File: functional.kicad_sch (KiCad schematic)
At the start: 12 parts, among them SW1 PCM12SMTR, U2 APX803L20-29SA-7, U3 PL500-37TC, Y1 XRCGB32M000F2P01R0

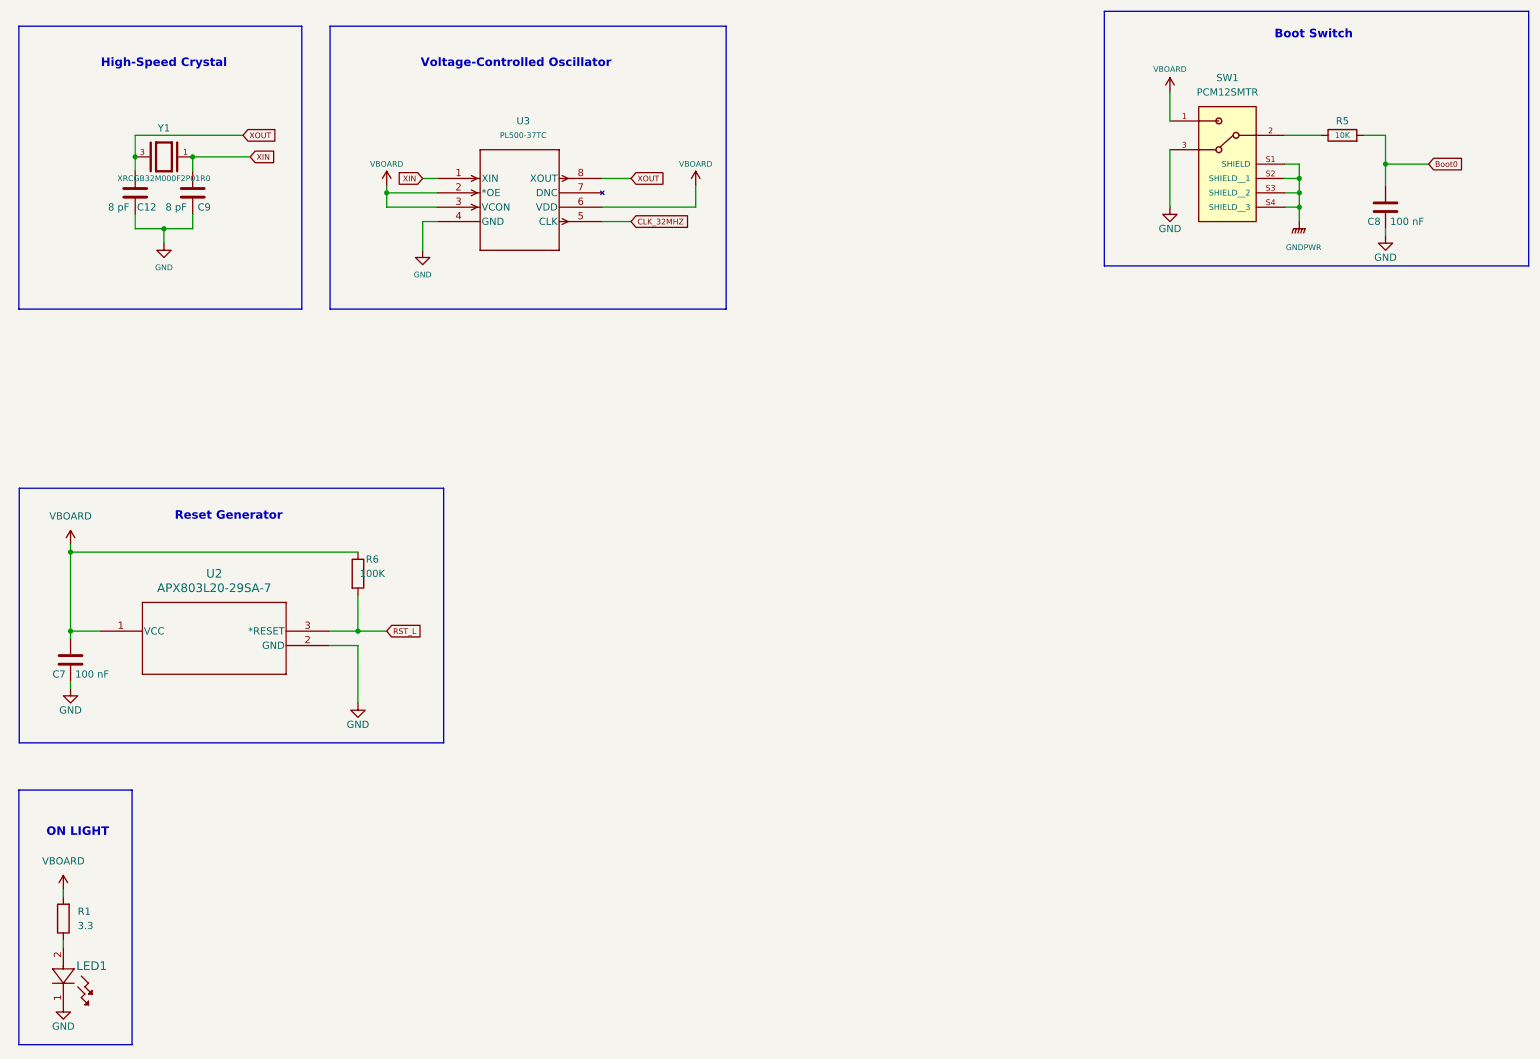
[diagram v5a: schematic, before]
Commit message: separated voltage source labels
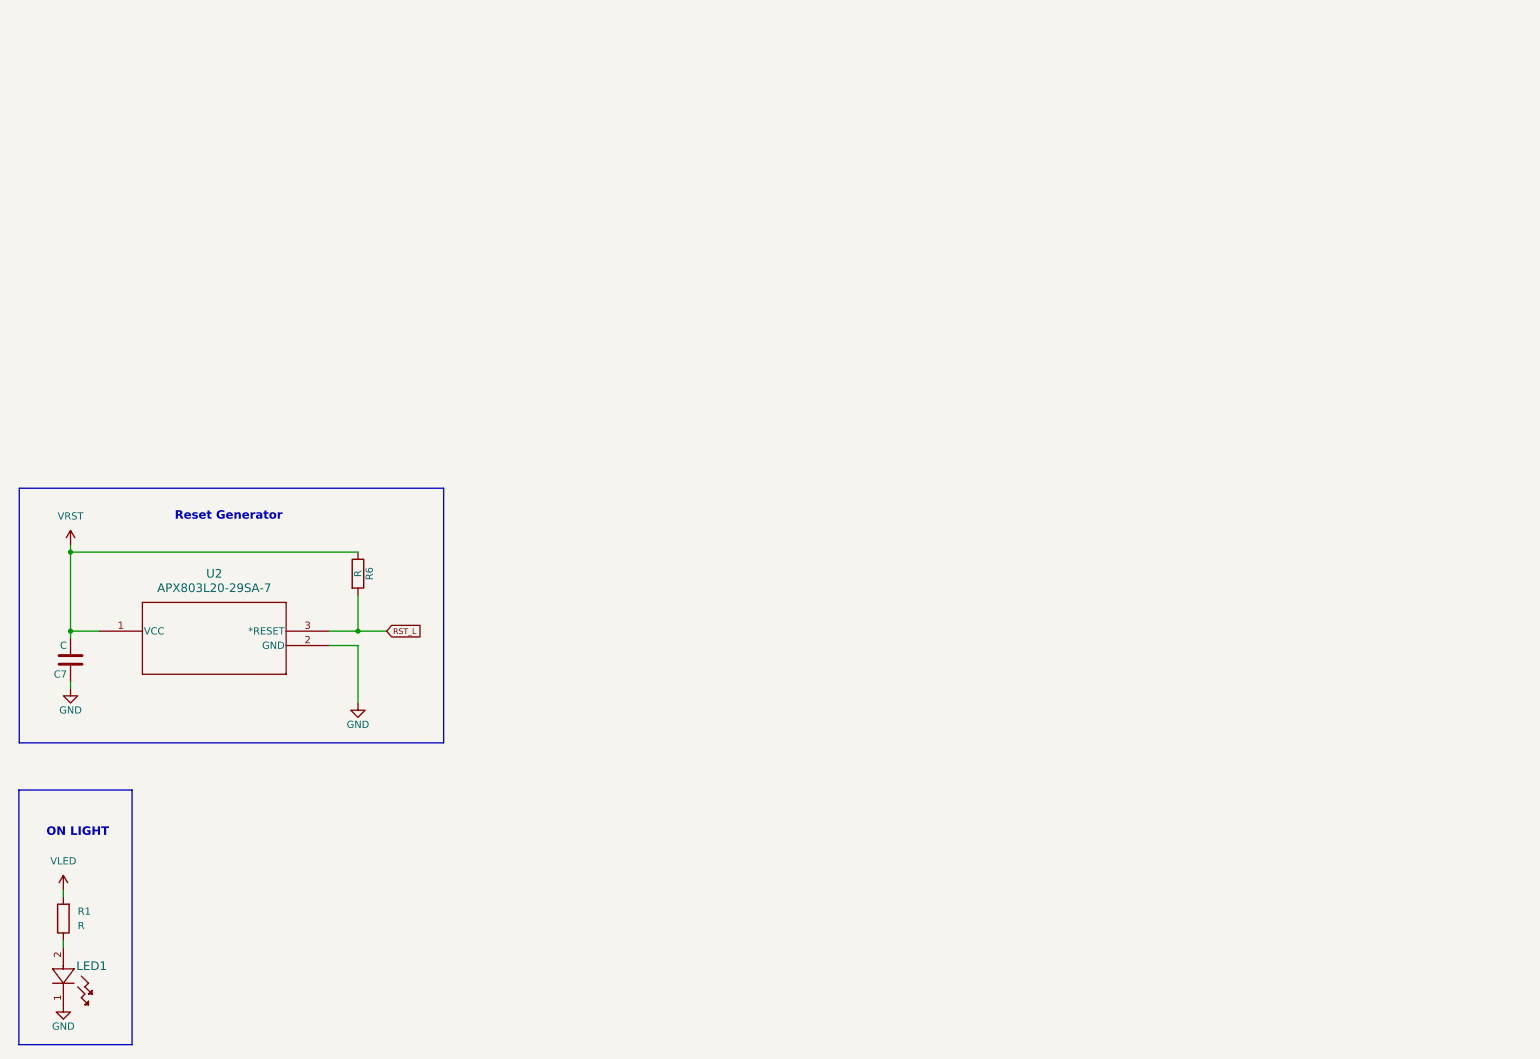
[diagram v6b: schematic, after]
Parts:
- removed C12, C9: 8 pF, Capacitor_SMD:C_0805_2012Metric, symbol Device:C
- removed C8: 100 nF, Capacitor_SMD:C_0805_2012Metric, symbol Device:C
- removed R5: 10K, Resistor_SMD:R_0805_2012Metric, symbol Device:R
- removed SW1: PCM12SMTR, PCM12SMTR:PCM12SMTR_CNK, symbol PCM12SMTR:PCM12SMTR
- removed U3: PL500-37TC, SOP-8_MCH, symbol VCO_36MHZ:PL500-37TC
- removed Y1: XRCGB32M000F2P01R0, XRCGB32M000F2P01R0:OSC_XRCGB32M000F2P01R0, symbol XRCGB32M000F2P01R0:XRCGB32M000F2P01R0
- C7: value 100 nF -> C
- R1: value 3.3 -> R
- R6: value 100K -> R
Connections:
- net VBOARD renamed VRST
- net VRST: no longer R1.2
- new net VLED: R1.2
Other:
- note removed: "Boot Switch"
- note removed: "High-Speed Crystal"
- note removed: "Voltage-Controlled Oscillator"

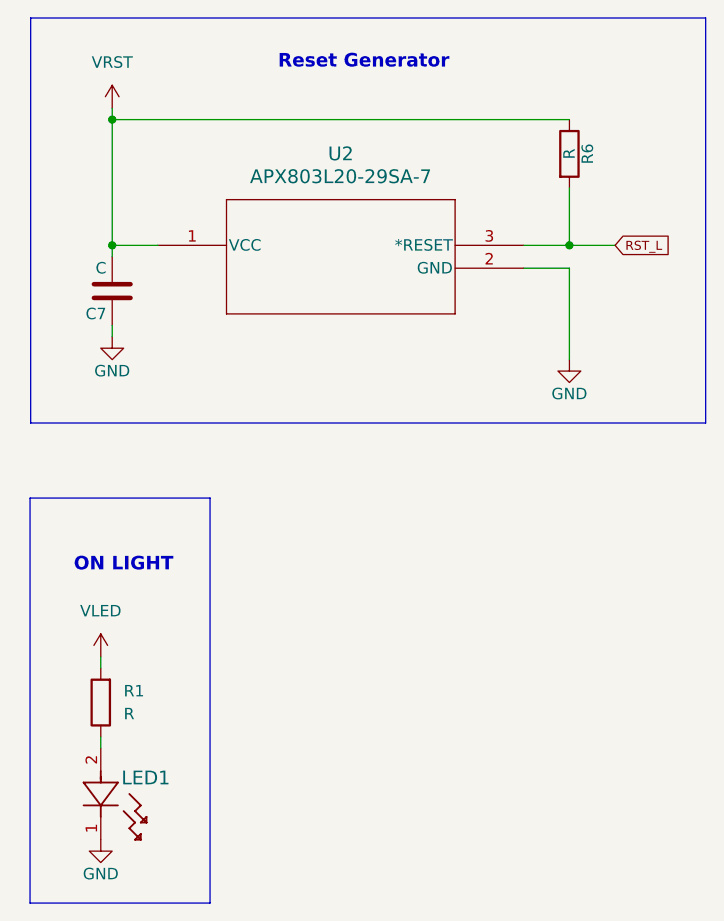
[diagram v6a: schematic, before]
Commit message: isolated v sources
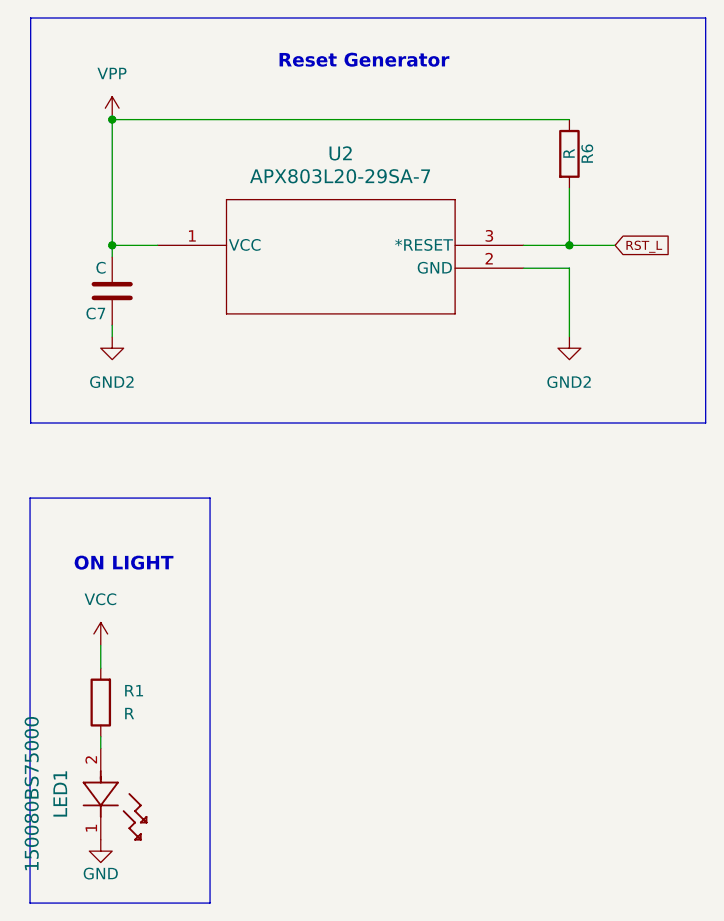
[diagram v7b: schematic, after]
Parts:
- LED1: footprint 150080BS75000:150080BS75000 -> LED_BS75000_WRE; symbol 150080BS75000:150080BS75000 -> LED_0885:150080BS75000
- U2: footprint APX803L20-29-SA-7:SOT23_SA_DIO -> SOT23_SA_DIO; symbol APX803L20_29SA_7:APX803L20-29SA-7 -> PMIC_SUPERVISOR:APX803L20-29SA-7
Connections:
- net GND: no longer C7.1, U2.2 (GND)
- net VLED renamed VCC
- net VRST renamed VPP
- new net GND2: C7.1, U2.2 (GND)

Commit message: added sheets
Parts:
- LED1: footprint LED_BS75000_WRE -> LED_0805_BLUE:150080BS75000
- U2: footprint SOT23_SA_DIO -> PMIC_SUPERVISOR_1CH:SOT23_SA_DIO
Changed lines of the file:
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@@
 			)
 		)
-		(property "Footprint" "LED_BS75000_WRE"
+		(property "Footprint" "LED_0805_BLUE:150080BS75000"
 			(at 18.288 170.434 0)
 			(effects
@@
 			)
 		)
-		(property "Footprint" "SOT23_SA_DIO"
+		(property "Footprint" "PMIC_SUPERVISOR_1CH:SOT23_SA_DIO"
 			(at 29.21 121.92 0)
 			(effects
